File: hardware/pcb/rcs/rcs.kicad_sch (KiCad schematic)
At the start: 28 parts, among them J1 UART, Q1 BS170, Q2 BS170, Q3 BS170, Q4 BS170, Q5 BS170, Q6 BS170, U1 ESP32

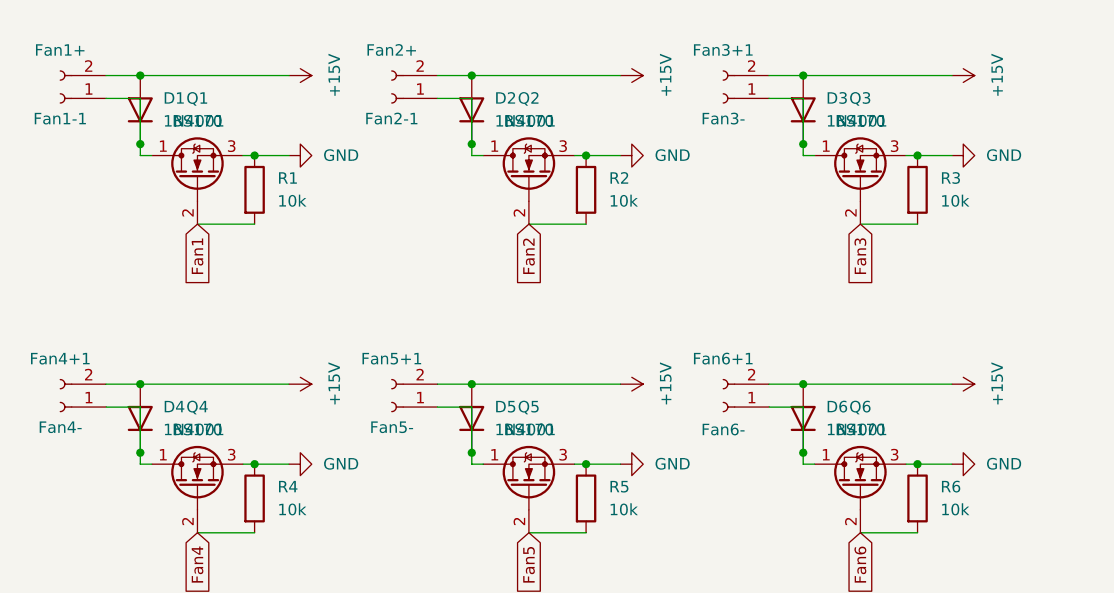
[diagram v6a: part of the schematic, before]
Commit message: Fix flyback diode orientation, round pcb corners
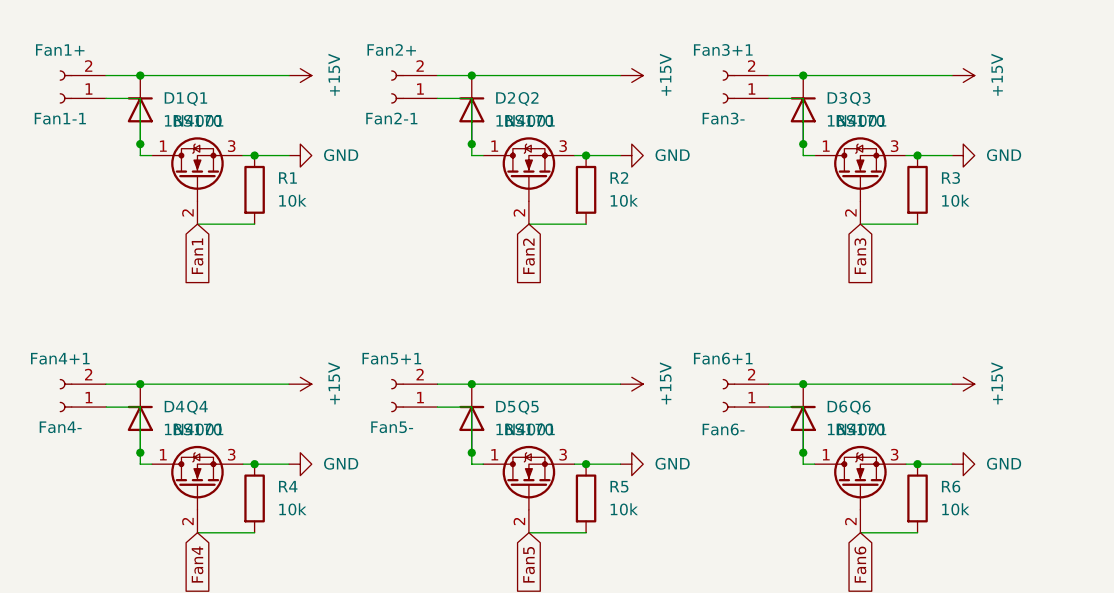
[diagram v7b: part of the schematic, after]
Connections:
- net +15V: now also D1.1 (K), D2.1 (K), D3.1 (K), D4.1 (K), D5.1 (K), D6.1 (K); no longer D1.2 (A), D2.2 (A), D3.2 (A), D4.2 (A), D5.2 (A), D6.2 (A)
- net at Fan6+1.1 (Pin_1), Q6.1 (D): now also D6.2 (A); no longer D6.1 (K)
- net at Fan2-1.1 (Pin_1), Q2.1 (D): now also D2.2 (A); no longer D2.1 (K)
- net at Fan5+1.1 (Pin_1), Q5.1 (D): now also D5.2 (A); no longer D5.1 (K)
- net at Fan3+1.1 (Pin_1), Q3.1 (D): now also D3.2 (A); no longer D3.1 (K)
- net at Fan1-1.1 (Pin_1), Q1.1 (D): now also D1.2 (A); no longer D1.1 (K)
- net at Fan4+1.1 (Pin_1), Q4.1 (D): now also D4.2 (A); no longer D4.1 (K)
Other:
- moved on the sheet: D1, D2, D3, D4, D5, D6
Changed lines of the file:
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@@
 	(paper "A4")
 	(junction
-		(at 109.22 59.69)
+		(at 35.56 59.69)
 		(diameter 0)
 		(color 0 0 0 0)
 	)
 	(junction
-		(at 72.39 67.31)
+		(at 72.39 59.69)
 		(diameter 0)
 		(color 0 0 0 0)
 	)
 	(junction
-		(at 35.56 67.31)
+		(at 35.56 25.4)
 		(diameter 0)
 		(color 0 0 0 0)
@@
 	)
 	(junction
-		(at 109.22 25.4)
+		(at 72.39 67.31)
 		(diameter 0)
 		(color 0 0 0 0)
 	)
 	(junction
-		(at 35.56 25.4)
+		(at 35.56 33.02)
 		(diameter 0)
 		(color 0 0 0 0)
 	)
 	(junction
-		(at 35.56 33.02)
+		(at 121.92 34.29)
 		(diameter 0)
 		(color 0 0 0 0)
 	)
 	(junction
-		(at 109.22 33.02)
+		(at 72.39 33.02)
 		(diameter 0)
 		(color 0 0 0 0)
 	)
 	(junction
-		(at 72.39 25.4)
+		(at 48.26 68.58)
 		(diameter 0)
 		(color 0 0 0 0)
 	)
 	(junction
-		(at 121.92 34.29)
+		(at 109.22 33.02)
 		(diameter 0)
 		(color 0 0 0 0)
 	)
 	(junction
-		(at 48.26 68.58)
+		(at 35.56 67.31)
 		(diameter 0)
 		(color 0 0 0 0)
 	)
 	(junction
-		(at 72.39 59.69)
+		(at 109.22 59.69)
 		(diameter 0)
 		(color 0 0 0 0)
 	)
 	(junction
-		(at 35.56 59.69)
+		(at 85.09 34.29)
 		(diameter 0)
 		(color 0 0 0 0)
 	)
 	(junction
-		(at 85.09 34.29)
+		(at 109.22 25.4)
 		(diameter 0)
 		(color 0 0 0 0)
@@
 	)
 	(junction
-		(at 72.39 33.02)
+		(at 85.09 68.58)
 		(diameter 0)
 		(color 0 0 0 0)
 	)
 	(junction
-		(at 85.09 68.58)
+		(at 48.26 34.29)
 		(diameter 0)
 		(color 0 0 0 0)
 	)
 	(junction
-		(at 48.26 34.29)
+		(at 72.39 25.4)
 		(diameter 0)
 		(color 0 0 0 0)
@@
 	(wire
 		(pts
-			(xy 72.39 27.94) (xy 72.39 33.02)
+			(xy 72.39 33.02) (xy 72.39 34.29)
 		)
 		(stroke
@@
 	(wire
 		(pts
-			(xy 109.22 59.69) (xy 105.41 59.69)
+			(xy 105.41 59.69) (xy 109.22 59.69)
 		)
 		(stroke
@@
 	(wire
 		(pts
-			(xy 35.56 25.4) (xy 31.75 25.4)
+			(xy 109.22 33.02) (xy 109.22 34.29)
 		)
 		(stroke
@@
 	(wire
 		(pts
-			(xy 35.56 67.31) (xy 35.56 68.58)
+			(xy 31.75 25.4) (xy 35.56 25.4)
 		)
 		(stroke
@@
 	(wire
 		(pts
-			(xy 48.26 34.29) (xy 52.07 34.29)
+			(xy 72.39 25.4) (xy 88.9 25.4)
 		)
 		(stroke
@@
 	(wire
 		(pts
-			(xy 109.22 67.31) (xy 109.22 68.58)
+			(xy 48.26 34.29) (xy 52.07 34.29)
 		)
 		(stroke
@@
 	(wire
 		(pts
-			(xy 115.57 41.91) (xy 121.92 41.91)
+			(xy 109.22 62.23) (xy 109.22 67.31)
 		)
 		(stroke
@@
 	(wire
 		(pts
-			(xy 125.73 25.4) (xy 109.22 25.4)
+			(xy 115.57 41.91) (xy 121.92 41.91)
 		)
 		(stroke
@@
 	(wire
 		(pts
-			(xy 72.39 62.23) (xy 72.39 67.31)
+			(xy 72.39 59.69) (xy 88.9 59.69)
 		)
 		(stroke
@@
 	(wire
 		(pts
-			(xy 109.22 33.02) (xy 109.22 34.29)
+			(xy 35.56 67.31) (xy 35.56 68.58)
 		)
 		(stroke
@@
 	(wire
 		(pts
-			(xy 72.39 67.31) (xy 72.39 68.58)
+			(xy 35.56 59.69) (xy 52.07 59.69)
 		)
 		(stroke
@@
 	(wire
 		(pts
-			(xy 109.22 62.23) (xy 109.22 67.31)
+			(xy 72.39 62.23) (xy 72.39 67.31)
 		)
 		(stroke
@@
 	(wire
 		(pts
-			(xy 125.73 59.69) (xy 109.22 59.69)
-		)
-		(stroke
-			(width 0)
-			(type default)
-		)
-	)
-	(wire
-		(pts
 			(xy 121.92 34.29) (xy 125.73 34.29)
 		)
@@
 	(wire
 		(pts
-			(xy 52.07 25.4) (xy 35.56 25.4)
+			(xy 46.99 68.58) (xy 48.26 68.58)
 		)
 		(stroke
@@
 	(wire
 		(pts
-			(xy 46.99 68.58) (xy 48.26 68.58)
+			(xy 109.22 68.58) (xy 110.49 68.58)
 		)
 		(stroke
@@
 	(wire
 		(pts
-			(xy 109.22 68.58) (xy 110.49 68.58)
+			(xy 181.61 31.75) (xy 186.69 31.75)
 		)
 		(stroke
@@
 	(wire
 		(pts
-			(xy 181.61 31.75) (xy 186.69 31.75)
+			(xy 109.22 25.4) (xy 125.73 25.4)
 		)
 		(stroke
@@
 	(wire
 		(pts
-			(xy 72.39 33.02) (xy 72.39 34.29)
+			(xy 72.39 27.94) (xy 72.39 33.02)
 		)
 		(stroke
@@
 	(wire
 		(pts
+			(xy 35.56 33.02) (xy 35.56 34.29)
+		)
+		(stroke
+			(width 0)
+			(type default)
+		)
+	)
+	(wire
+		(pts
 			(xy 186.69 39.37) (xy 186.69 34.29)
 		)
@@
 	(wire
 		(pts
-			(xy 35.56 59.69) (xy 31.75 59.69)
+			(xy 31.75 59.69) (xy 35.56 59.69)
 		)
 		(stroke
@@
 	(wire
 		(pts
-			(xy 72.39 25.4) (xy 68.58 25.4)
+			(xy 68.58 25.4) (xy 72.39 25.4)
 		)
 		(stroke
@@
 	(wire
 		(pts
-			(xy 72.39 59.69) (xy 68.58 59.69)
+			(xy 68.58 59.69) (xy 72.39 59.69)
 		)
 		(stroke
@@
 	(wire
 		(pts
-			(xy 88.9 59.69) (xy 72.39 59.69)
+			(xy 121.92 68.58) (xy 125.73 68.58)
 		)
 		(stroke
@@
 	(wire
 		(pts
-			(xy 35.56 33.02) (xy 35.56 34.29)
+			(xy 72.39 67.31) (xy 72.39 68.58)
 		)
 		(stroke
@@
 	(wire
 		(pts
-			(xy 121.92 68.58) (xy 125.73 68.58)
+			(xy 68.58 27.94) (xy 72.39 27.94)
 		)
 		(stroke
@@
 	(wire
 		(pts
-			(xy 68.58 27.94) (xy 72.39 27.94)
+			(xy 68.58 62.23) (xy 72.39 62.23)
 		)
 		(stroke
@@
 	(wire
 		(pts
-			(xy 68.58 62.23) (xy 72.39 62.23)
+			(xy 48.26 68.58) (xy 52.07 68.58)
 		)
 		(stroke
@@
 	(wire
 		(pts
-			(xy 52.07 59.69) (xy 35.56 59.69)
+			(xy 105.41 25.4) (xy 109.22 25.4)
 		)
 		(stroke
@@
 	(wire
 		(pts
-			(xy 48.26 68.58) (xy 52.07 68.58)
+			(xy 115.57 76.2) (xy 121.92 76.2)
 		)
 		(stroke
@@
 	(wire
 		(pts
-			(xy 109.22 25.4) (xy 105.41 25.4)
+			(xy 109.22 59.69) (xy 125.73 59.69)
 		)
 		(stroke
@@
 	(wire
 		(pts
-			(xy 115.57 76.2) (xy 121.92 76.2)
+			(xy 31.75 62.23) (xy 35.56 62.23)
 		)
 		(stroke
@@
 	(wire
 		(pts
-			(xy 88.9 25.4) (xy 72.39 25.4)
+			(xy 109.22 67.31) (xy 109.22 68.58)
 		)
 		(stroke
@@
 	(wire
 		(pts
-			(xy 31.75 62.23) (xy 35.56 62.23)
+			(xy 35.56 25.4) (xy 52.07 25.4)
 		)
 		(stroke
@@
 	(symbol
 		(lib_id "Diode:1N4001")
-		(at 109.22 63.5 90)
+		(at 109.22 63.5 270)
 		(unit 1)
 		(exclude_from_sim no)
@@
 					(size 1.27 1.27)
 				)
-				(justify right)
+				(justify left)
 			)
 		)
@@
 					(size 1.27 1.27)
 				)
-				(justify right)
+				(justify left)
 			)
 		)
@@
 	(symbol
 		(lib_id "Diode:1N4001")
-		(at 35.56 29.21 90)
+		(at 35.56 29.21 270)
 		(unit 1)
 		(exclude_from_sim no)
@@
 					(size 1.27 1.27)
 				)
-				(justify right)
+				(justify left)
 			)
 		)
@@
 					(size 1.27 1.27)
 				)
-				(justify right)
+				(justify left)
 			)
 		)
@@
 	(symbol
 		(lib_id "Diode:1N4001")
-		(at 72.39 63.5 90)
+		(at 72.39 63.5 270)
 		(unit 1)
 		(exclude_from_sim no)
@@
 					(size 1.27 1.27)
 				)
-				(justify right)
+				(justify left)
 			)
 		)
@@
 					(size 1.27 1.27)
 				)
-				(justify right)
+				(justify left)
 			)
 		)
@@
 	(symbol
 		(lib_id "Diode:1N4001")
-		(at 35.56 63.5 90)
+		(at 35.56 63.5 270)
 		(unit 1)
 		(exclude_from_sim no)
@@
 					(size 1.27 1.27)
 				)
-				(justify right)
+				(justify left)
 			)
 		)
@@
 					(size 1.27 1.27)
 				)
-				(justify right)
+				(justify left)
 			)
 		)
@@
 	(symbol
 		(lib_id "Diode:1N4001")
-		(at 109.22 29.21 90)
+		(at 109.22 29.21 270)
 		(unit 1)
 		(exclude_from_sim no)
@@
 					(size 1.27 1.27)
 				)
-				(justify right)
+				(justify left)
 			)
 		)
@@
 					(size 1.27 1.27)
 				)
-				(justify right)
+				(justify left)
 			)
 		)
@@
 	(symbol
 		(lib_id "Diode:1N4001")
-		(at 72.39 29.21 90)
+		(at 72.39 29.21 270)
 		(unit 1)
 		(exclude_from_sim no)
@@
 					(size 1.27 1.27)
 				)
-				(justify right)
+				(justify left)
 			)
 		)
@@
 					(size 1.27 1.27)
 				)
-				(justify right)
+				(justify left)
 			)
 		)
